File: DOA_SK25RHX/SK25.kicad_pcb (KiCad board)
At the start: 2 copper layers, 42.5 x 30 mm, 41 parts, among them J1 Imput-, J2 Input+, J3 V+, J4 Output, J5 V-, J6 GND, Q1 BC560C, Q10 BD140, Q2 KSA992, Q3 KSA992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

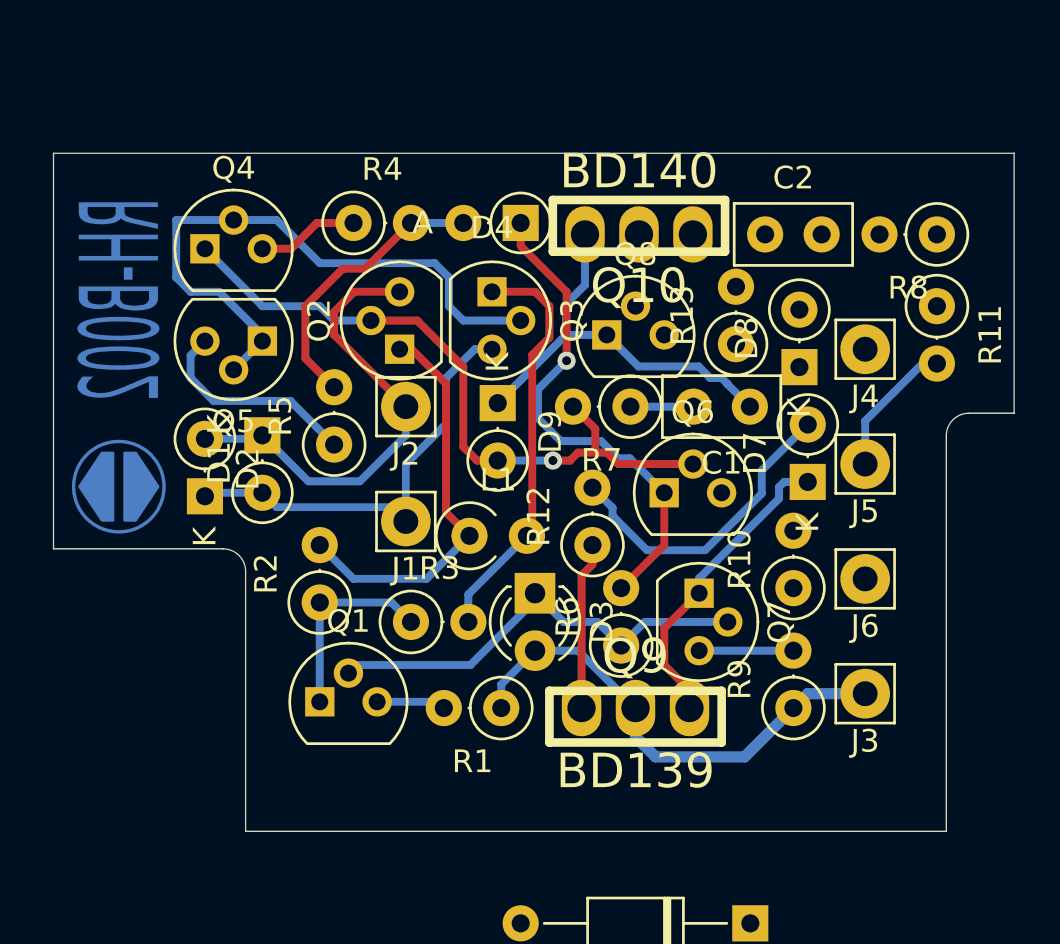
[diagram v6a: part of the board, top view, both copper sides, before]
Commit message: completed routing, except diose pads
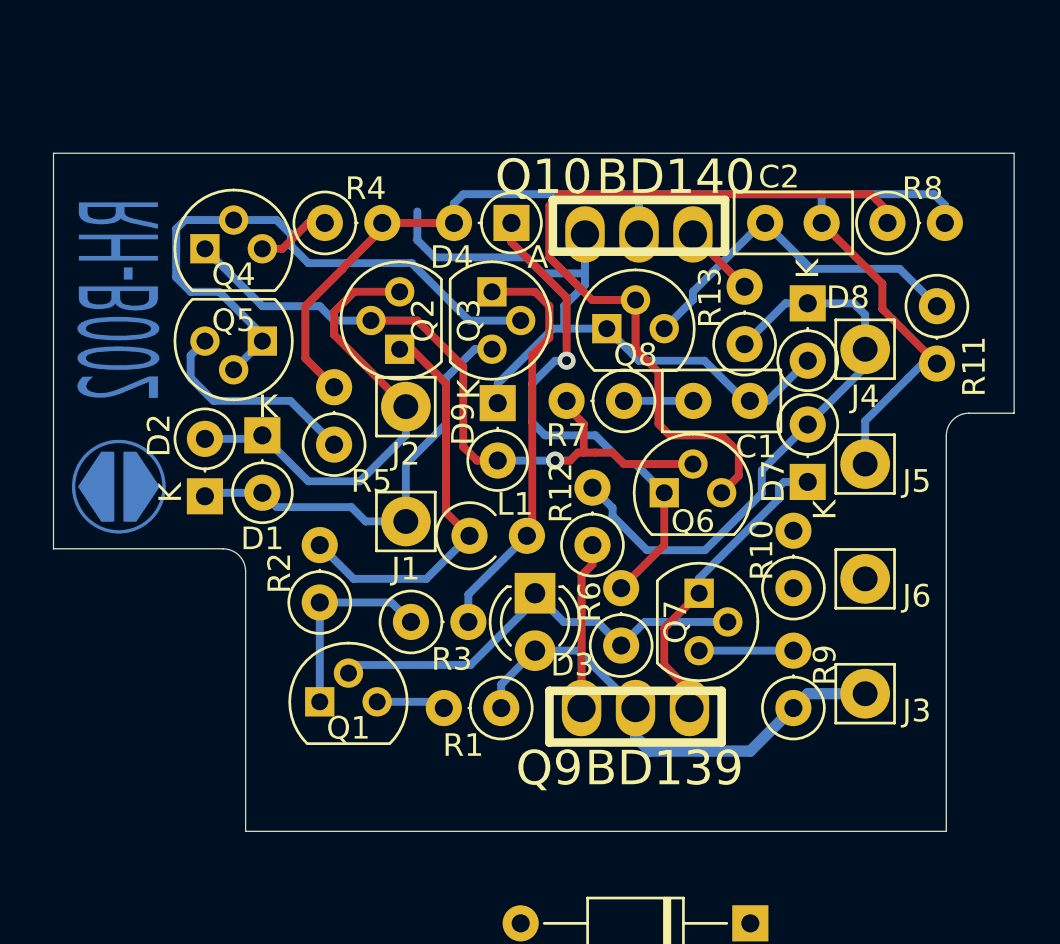
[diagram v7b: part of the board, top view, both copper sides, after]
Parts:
- J1: value Imput- -> Input-
- moved D8 2.85 mm to (166.4, 88.1), turned to -90 degrees
- moved R8 2.25 mm to (169.9, 84.6), turned to 0 degrees
- moved R4 1.27 mm to (145.0, 84.6)
- moved C2 0.51 mm to (164.5, 84.6)
- moved D4 0.41 mm to (153.3, 84.6)
- moved R13 0.38 mm to (163.6, 89.9)
- moved R7 0.38 mm to (158.2, 92.5)
- moved Q8 0.27 mm to (157.5, 89.3)
- moved C1 0.25 mm to (163.8, 92.5)
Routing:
- net Net-(Q6-Pad3): track 0.00 -> 35.0 mm
- net Net-(C2-Pad2): track 18.8 -> 53.6 mm
- net Net-(C2-Pad1): track 0.00 -> 15.7 mm
- net Net-(C1-Pad1): track 18.5 -> 31.5 mm
- net Net-(D7-Pad2): track 13.8 -> 26.0 mm
- net Net-(Q10-Pad1): track 0.00 -> 3.26 mm
- net Net-(Q4-Pad3): track 4.51 -> 3.49 mm
- net Net-(D4-Pad1): track 22.0 -> 22.9 mm
- net Net-(Q3-Pad2): track 27.3 -> 26.6 mm

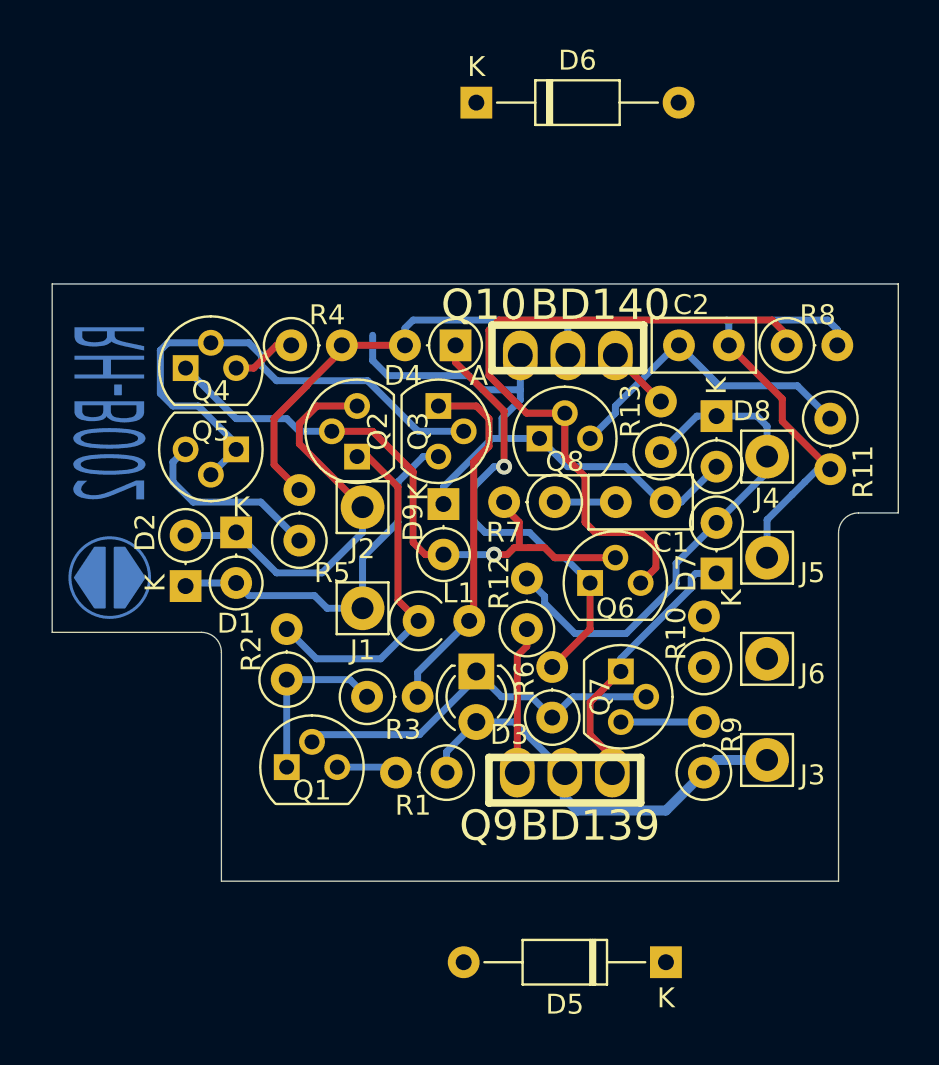
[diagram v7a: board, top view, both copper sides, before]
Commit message: completed routing, added solder pads and solder mask clearance
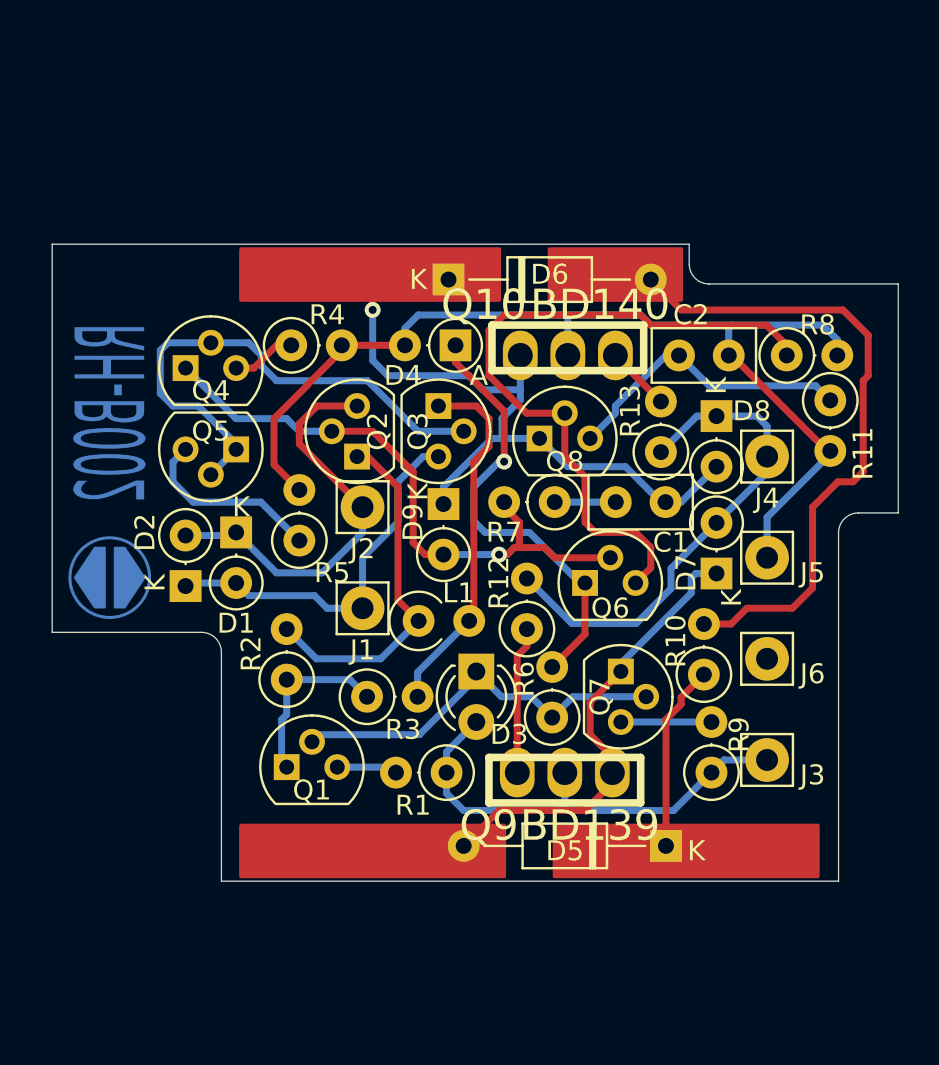
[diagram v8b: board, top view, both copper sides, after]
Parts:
- moved D6 9.00 mm to (152.9, 81.3)
- moved D5 5.84 mm to (163.8, 109.7)
- moved R11 0.92 mm to (172.1, 87.3)
- moved C2 0.51 mm to (164.5, 85.1)
- moved R8 0.51 mm to (169.9, 85.1)
- moved R10 0.38 mm to (165.7, 101.1)
- moved R9 0.38 mm to (166.1, 106.0)
- moved Q6 0.25 mm to (159.8, 96.5)
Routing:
- net Net-(D6-Pad2): track 0.00 -> 32.6 mm
- net Net-(D5-Pad2): track 13.7 -> 23.8 mm
- net Net-(D5-Pad1): track 0.00 -> 9.40 mm
- net Net-(C1-Pad1): track 31.5 -> 37.9 mm, vias 0 -> 1
- net Net-(D3-Pad2): track 21.4 -> 23.8 mm
- net Net-(C2-Pad1): track 15.7 -> 15.1 mm
- net Net-(D7-Pad2): track 26.0 -> 25.3 mm
- net Net-(D4-Pad1): track 22.9 -> 22.4 mm
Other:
- board size 42.5 x 30 mm -> 42.5 x 32 mm
